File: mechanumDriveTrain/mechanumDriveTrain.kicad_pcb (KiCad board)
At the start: 4 copper layers, 11 parts, among them IC1 TCAN3414DR, J1 XT30U-M, J2 BM02B-SRSS-TB, J3 Conn_01x08, J4 Conn_01x08, U1 Teensy 4.1

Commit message: Cleaned up schematic, added LDO regulator for 5v to mechanum board
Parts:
- added C3: 0.1 uF, Capacitor_SMD:C_0805_2012Metric_Pad1.18x1.45mm_HandSolder, F.Cu at (74.3, 63.3)
- added C4: 0.1 uF, Capacitor_SMD:C_0805_2012Metric_Pad1.18x1.45mm_HandSolder, F.Cu at (70.9, 57.6)
- added C5: 10 uF, Capacitor_SMD:C_0805_2012Metric_Pad1.18x1.45mm_HandSolder, F.Cu at (68.8, 57.6)
- added C6: 0.1 uF, Capacitor_SMD:C_0805_2012Metric_Pad1.18x1.45mm_HandSolder, F.Cu at (32.7, 30.6)
- added U2: LD1117S50TR_SOT223, Package_TO_SOT_SMD:SOT-223-3_TabPin2, F.Cu at (76.4, 58.6)
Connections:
- U1 pad 3.3V_1: Net-(U1-3.3V-Pad3.3V_1) -> unconnected-(U1-3.3V-Pad3.3V_1)
- U1 pad 3.3V_2: Net-(U1-3.3V-Pad3.3V_1) -> unconnected-(U1-3.3V-Pad3.3V_1)_2
- U1 pad 3.3V_3: Net-(U1-3.3V-Pad3.3V_1) -> unconnected-(U1-3.3V-Pad3.3V_1)_1
- U1 pad VIN: unconnected-(U1-PadVIN) -> +5V

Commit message: Added step for tano
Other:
- board outline added: 65 x 51 mm
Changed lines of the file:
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@@
 		)
 	)
+	(gr_rect
+		(start 28 28)
+		(end 93 79)
+		(stroke
+			(width 0.05)
+			(type default)
+		)
+		(fill none)
+		(layer "Edge.Cuts")
+	)
 )

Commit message: Added a 2nd pololu board
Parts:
- added J5: Conn_01x08, Connector_PinSocket_2.54mm:PinSocket_1x08_P2.54mm_Vertical, F.Cu at (31.3, 82.8)
- added J6: Conn_01x08, Connector_PinSocket_2.54mm:PinSocket_1x08_P2.54mm_Vertical, F.Cu at (59.2, 82.8)
- added R4: 60, Resistor_SMD:R_0805_2012Metric_Pad1.20x1.40mm_HandSolder, F.Cu at (86.1, 30.5)
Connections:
- net DIR renamed DIR1
- net FLT renamed FLT1
- net OUTA renamed OUTA1
- net OUTB renamed OUTB1
- net PWM renamed PWM1
- net SLP renamed SLP1
- U1 pad 28: unconnected-(U1-RX7-Pad28) -> PWM2
- U1 pad 29: unconnected-(U1-TX7-Pad29) -> DIR2
- U1 pad 34: unconnected-(U1-RX8-Pad34) -> SLP2
- U1 pad 35: unconnected-(U1-TX8-Pad35) -> FLT2
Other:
- board size 65 x 51 mm -> 66.9 x 83 mm

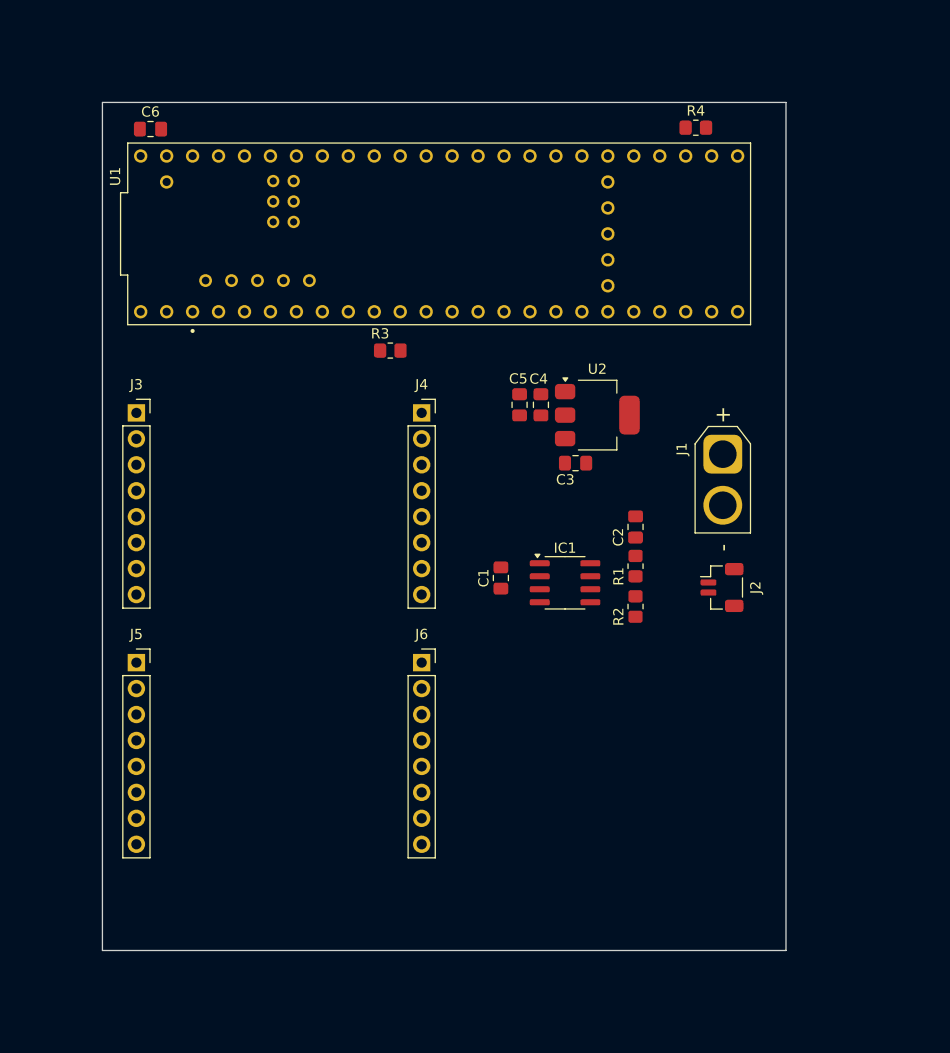
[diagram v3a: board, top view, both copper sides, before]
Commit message: create symbol and footprint for the Pololu 18v17 motor controller
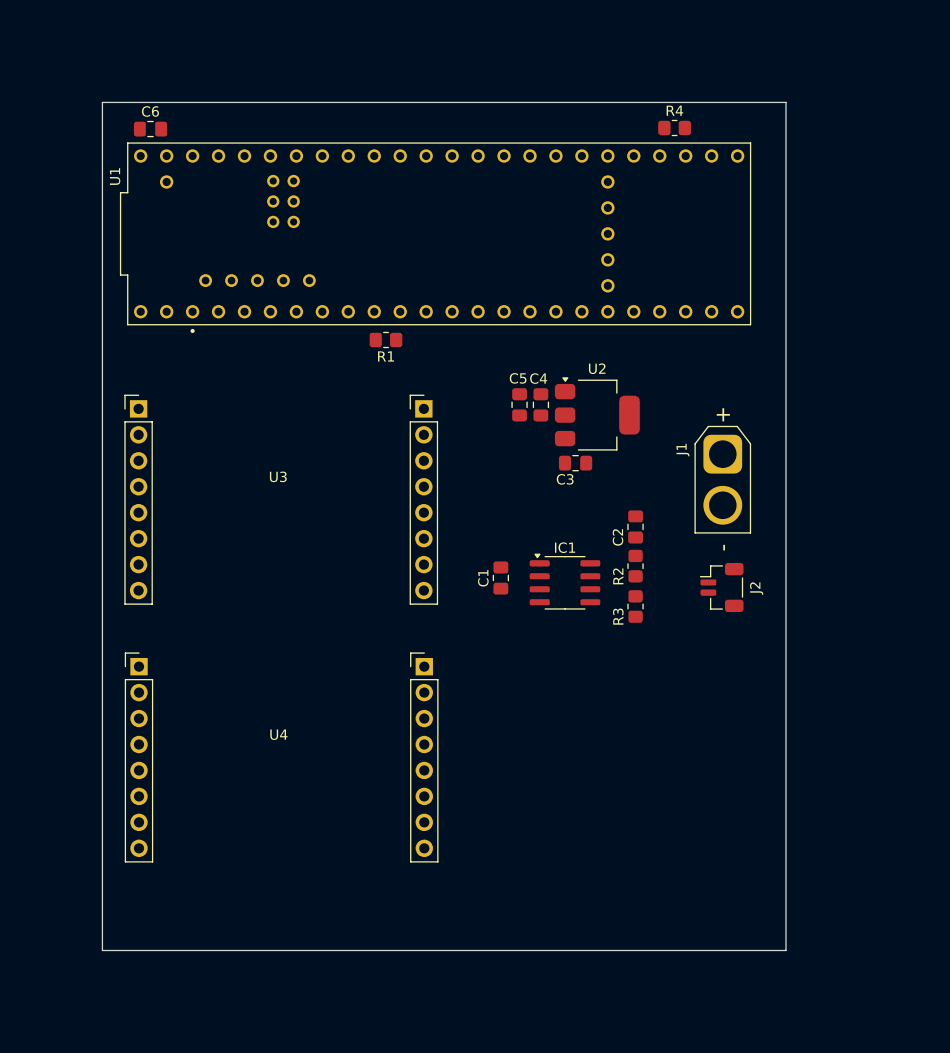
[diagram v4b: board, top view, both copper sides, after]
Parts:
- removed J3, J4, J5, J6: Conn_01x08, Connector_PinSocket_2.54mm:PinSocket_1x08_P2.54mm_Vertical
- removed the R3 at (56.2, 52.3)
- added R1: 60, Resistor_SMD:R_0805_2012Metric_Pad1.20x1.40mm_HandSolder, F.Cu at (55.8, 51.2)
- added U3: ~, PolouMotorDriver:Pololu_G2_Motor_Driver_18v17, F.Cu at (45.2, 51.2)
- added U4: ~, PolouMotorDriver:Pololu_G2_Motor_Driver_18v17, F.Cu at (45.2, 76.4)
- moved R4 2.08 mm to (84.0, 30.5)
- renumbered R1 to R2, R2 to R3
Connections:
- R4 pad 1: FLT2 -> +3V3
- R4 pad 2: +3V3 -> FLT2

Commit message: Added connectors for motos, added schematic
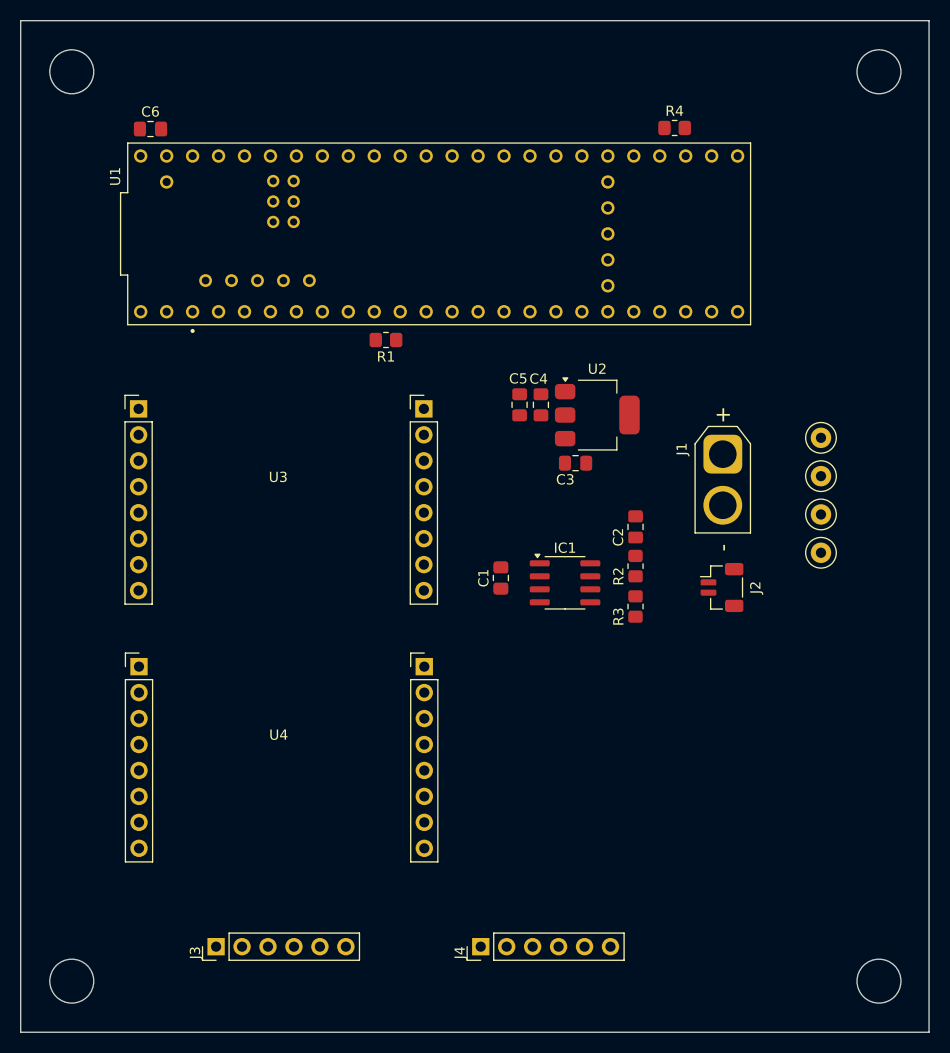
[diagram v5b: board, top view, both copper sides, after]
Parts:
- added H1: M4, MountingHole:MountingHole_4.3mm_M4_DIN965, F.Cu at (25.0, 25.0)
- added H2: M4, MountingHole:MountingHole_4.3mm_M4_DIN965, F.Cu at (104.0, 25.0)
- added H3: M4, MountingHole:MountingHole_4.3mm_M4_DIN965, F.Cu at (25.0, 114.0)
- added H4: M4, MountingHole:MountingHole_4.3mm_M4_DIN965, F.Cu at (104.0, 114.0)
- added J3: 5 pin dupont, Connector_PinHeader_2.54mm:PinHeader_1x06_P2.54mm_Vertical, F.Cu at (39.1, 110.6)
- added J4: 5 pin dupont, Connector_PinHeader_2.54mm:PinHeader_1x06_P2.54mm_Vertical, F.Cu at (65.0, 110.6)
- added TP1: ~, TestPoint:TestPoint_Loop_D1.80mm_Drill1.0mm_Beaded, F.Cu at (98.3, 60.8)
- added TP2: ~, TestPoint:TestPoint_Loop_D1.80mm_Drill1.0mm_Beaded, F.Cu at (98.3, 64.6)
- added TP3: ~, TestPoint:TestPoint_Loop_D1.80mm_Drill1.0mm_Beaded, F.Cu at (98.3, 68.3)
- added TP4: ~, TestPoint:TestPoint_Loop_D1.80mm_Drill1.0mm_Beaded, F.Cu at (98.3, 72.1)
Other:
- board size 66.9 x 83 mm -> 88.9 x 99 mm

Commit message: Updated schematic, started new layout of board
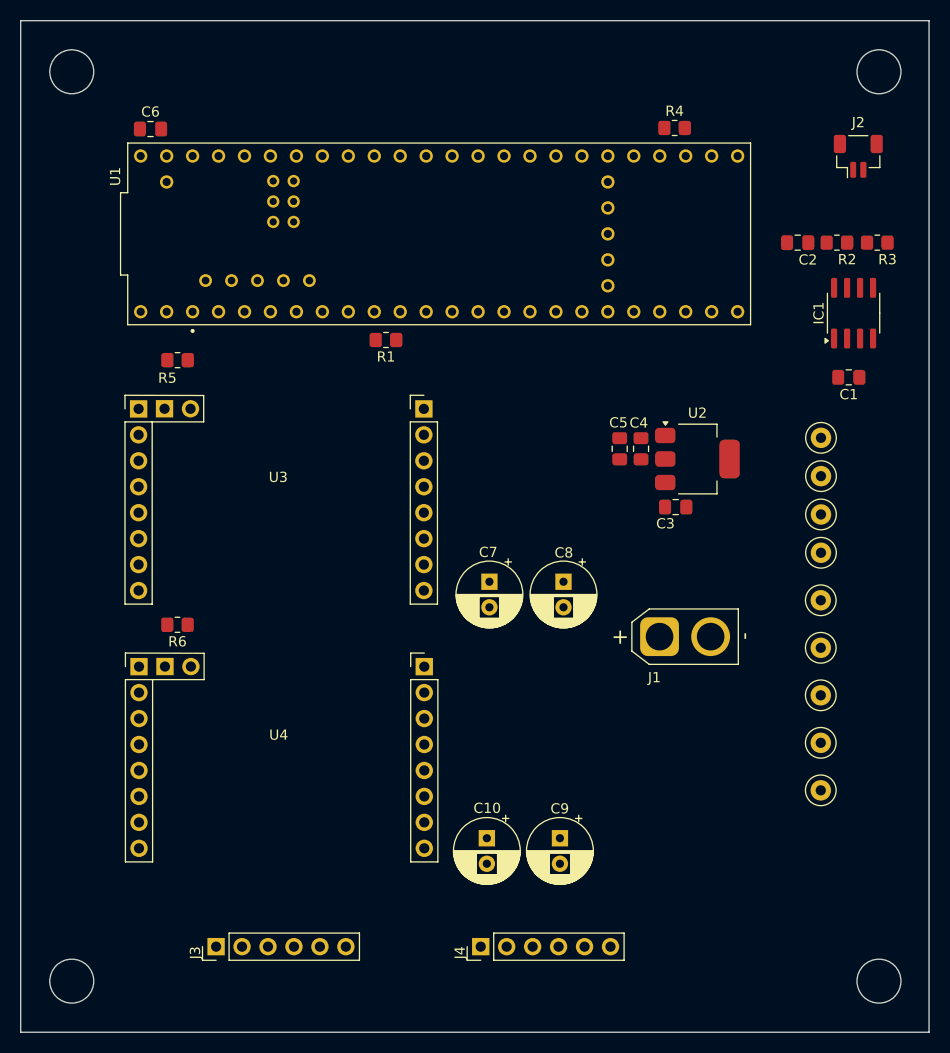
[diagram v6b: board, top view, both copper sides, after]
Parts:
- added C10: 220uF, Capacitor_THT:CP_Radial_D6.3mm_P2.50mm, F.Cu at (65.6, 100.0)
- added C7: 220uF, Capacitor_THT:CP_Radial_D6.3mm_P2.50mm, F.Cu at (65.9, 74.9)
- added C8: 220uF, Capacitor_THT:CP_Radial_D6.3mm_P2.50mm, F.Cu at (73.1, 74.9)
- added C9: 220uF, Capacitor_THT:CP_Radial_D6.3mm_P2.50mm, F.Cu at (72.8, 100.0)
- added R5: 20K, Resistor_SMD:R_0805_2012Metric_Pad1.20x1.40mm_HandSolder, F.Cu at (35.4, 53.2)
- added R6: 20K, Resistor_SMD:R_0805_2012Metric_Pad1.20x1.40mm_HandSolder, F.Cu at (35.3, 79.1)
- added TP5: ~, TestPoint:TestPoint_Loop_D1.80mm_Drill1.0mm_Beaded, F.Cu at (98.3, 76.7)
- added TP6: ~, TestPoint:TestPoint_Loop_D1.80mm_Drill1.0mm_Beaded, F.Cu at (98.3, 81.4)
- added TP7: ~, TestPoint:TestPoint_Loop_D1.80mm_Drill1.0mm_Beaded, F.Cu at (98.3, 86.0)
- added TP8: ~, TestPoint:TestPoint_Loop_D1.80mm_Drill1.0mm_Beaded, F.Cu at (98.3, 90.7)
- added TP9: ~, TestPoint:TestPoint_Loop_D1.80mm_Drill1.0mm_Beaded, F.Cu at (98.3, 95.3)
- moved J2 44.3 mm to (102.0, 33.3), turned to 0 degrees
- moved R3 42.8 mm to (103.8, 41.7), turned to 180 degrees
- moved C1 39.3 mm to (101.0, 54.9), turned to 180 degrees
- moved IC1 38.7 mm to (101.5, 48.6), turned to 90 degrees
- moved R2 37.3 mm to (99.9, 41.7), turned to 180 degrees
- moved C2 32.0 mm to (96.0, 41.7), turned to 180 degrees
- moved J1 18.9 mm to (82.5, 80.3), turned to 0 degrees
- moved C3 10.7 mm to (84.1, 67.6)
- moved C4 10.7 mm to (80.7, 61.9)
- moved C5 10.7 mm to (78.6, 61.9)
- moved U2 10.7 mm to (86.2, 62.9)
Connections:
- C3 pad 1: +12V -> VCC
- U2 pad 3: +12V -> VCC
- U3 pad 6: unconnected-(U3-CS-Pad6) -> CS1
- U3 pad 8: unconnected-(U3-VM-Pad8) -> VCC
- U4 pad 6: unconnected-(U4-CS-Pad6) -> CS1
- U4 pad 8: unconnected-(U4-VM-Pad8) -> VCC

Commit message: Added cs2
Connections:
- U4 pad 6: CS1 -> CS2
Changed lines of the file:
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@@
 	(net 77 "Net-(U4-VREFGND)")
 	(net 78 "CS1")
+	(net 79 "CS2")
 	(footprint "Resistor_SMD:R_0805_2012Metric_Pad1.20x1.40mm_HandSolder"
 		(layer "F.Cu")
@@
 		(tags "resistor handsolder")
 		(property "Reference" "R2"
-			(at -1 -1.65 360)
+			(at -1 -1.65 0)
 			(layer "F.SilkS")
 			(effects
@@
 		)
 		(property "Value" "60"
-			(at 0 1.65 360)
+			(at 0 1.65 0)
 			(layer "F.Fab")
 			(hide yes)
@@
 		)
 		(fp_text user "${REFERENCE}"
-			(at 0 0 360)
+			(at 0 0 0)
 			(layer "F.Fab")
 			(effects
@@
 		(tags "resistor handsolder")
 		(property "Reference" "R5"
-			(at 1 -1.75 360)
+			(at 1 -1.75 0)
 			(layer "F.SilkS")
 			(effects
@@
 		)
 		(property "Value" "20K"
-			(at 0 1.65 360)
+			(at 0 1.65 0)
 			(layer "F.Fab")
 			(hide yes)
@@
 		)
 		(fp_text user "${REFERENCE}"
-			(at 0 0 360)
+			(at 0 0 0)
 			(layer "F.Fab")
 			(effects
@@
 		(tags "RC Connector XT30")
 		(property "Reference" "J1"
-			(at -0.5 4 360)
+			(at -0.5 4 0)
 			(layer "F.SilkS")
 			(effects
@@
 		)
 		(property "Value" "XT30U-M"
-			(at 2.5 4 360)
+			(at 2.5 4 0)
 			(layer "F.Fab")
 			(hide yes)
@@
 		)
 		(fp_text user "+"
-			(at -3.85 0 360)
+			(at -3.85 0 0)
 			(layer "F.SilkS")
 			(effects
@@
 		)
 		(fp_text user "${REFERENCE}"
-			(at 2.5 0 360)
+			(at 2.5 0 0)
 			(layer "F.Fab")
 			(effects
@@
 		(tags "connector JST SH vertical")
 		(property "Reference" "J2"
-			(at 0 -3.3 360)
+			(at 0 -3.3 0)
 			(layer "F.SilkS")
 			(effects
@@
 		)
 		(property "Value" "BM02B-SRSS-TB"
-			(at 0 3.3 360)
+			(at 0 3.3 0)
 			(layer "F.Fab")
 			(hide yes)
@@
 		)
 		(fp_text user "${REFERENCE}"
-			(at 0 -0.25 360)
+			(at 0 -0.25 0)
 			(layer "F.Fab")
 			(effects
@@
 			(layers "*.Cu" "*.Mask")
 			(remove_unused_layers no)
-			(net 78 "CS1")
+			(net 79 "CS2")
 			(pinfunction "CS")
 			(pintype "output")
@@
 		(tags "capacitor handsolder")
 		(property "Reference" "C1"
-			(at 0 -1.68 360)
+			(at 0 -1.68 0)
 			(layer "F.SilkS")
 			(effects
@@
 		)
 		(property "Value" "0.1 uF"
-			(at 0 1.68 360)
+			(at 0 1.68 0)
 			(layer "F.Fab")
 			(hide yes)
@@
 		)
 		(fp_text user "${REFERENCE}"
-			(at 0 0 360)
+			(at 0 0 0)
 			(layer "F.Fab")
 			(effects
@@
 		(tags "resistor handsolder")
 		(property "Reference" "R3"
-			(at -1 -1.65 360)
+			(at -1 -1.65 0)
 			(layer "F.SilkS")
 			(effects
@@
 		)
 		(property "Value" "60"
-			(at 0 1.65 360)
+			(at 0 1.65 0)
 			(layer "F.Fab")
 			(hide yes)
@@
 		)
 		(fp_text user "${REFERENCE}"
-			(at 0 0 360)
+			(at 0 0 0)
 			(layer "F.Fab")
 			(effects
@@
 		(tags "capacitor handsolder")
 		(property "Reference" "C2"
-			(at -1 -1.68 360)
+			(at -1 -1.68 0)
 			(layer "F.SilkS")
 			(effects
@@
 		)
 		(property "Value" "560pF"
-			(at 0 1.68 360)
+			(at 0 1.68 0)
 			(layer "F.Fab")
 			(hide yes)
@@
 		)
 		(fp_text user "${REFERENCE}"
-			(at 0 0 360)
+			(at 0 0 0)
 			(layer "F.Fab")
 			(effects
@@
 		(tags "resistor handsolder")
 		(property "Reference" "R6"
-			(at 0 -1.65 360)
+			(at 0 -1.65 0)
 			(layer "F.SilkS")
 			(effects
@@
 		)
 		(property "Value" "20K"
-			(at 0 1.65 360)
+			(at 0 1.65 0)
 			(layer "F.Fab")
 			(hide yes)
@@
 		)
 		(fp_text user "${REFERENCE}"
-			(at 0 0 360)
+			(at 0 0 0)
 			(layer "F.Fab")
 			(effects

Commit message: add 3d model for second motor driver
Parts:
- moved U4 2.32 mm to (45.3, 78.7)
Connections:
- U1 pad 14: unconnected-(U1-A0-Pad14) -> CS1
- U1 pad 15: unconnected-(U1-A1-Pad15) -> CS2
- U1 pad 24: unconnected-(U1-A10-Pad24) -> EN_OUTA2
- U1 pad 25: unconnected-(U1-A11-Pad25) -> EN_OUTB2
- U1 pad 3: unconnected-(U1-LRCLK2-Pad3) -> EN_OUTA1
- U1 pad 4: unconnected-(U1-BCLK2-Pad4) -> EN_OUTB1
